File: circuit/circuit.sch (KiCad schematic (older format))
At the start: 13 parts, among them U1 LM324

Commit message: Added decoupling capacitors to diff amp circuit
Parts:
- added C1: 1uF, symbol Device:C_Small
- added C2: 0.1uF, symbol Device:C_Small
- R3, R4: value 50K -> 10K
- R7, R8: value 50K -> 1K
- gave numbers to parts that had none: 1
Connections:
- net GND: now also C1.2, C2.2
- net VCC: now also C1.1, C2.1
- net at R4.1, R7.2: now also U1.6 (-); no longer U1.5 (+)
- net at R3.1, R8.2: now also U1.5 (+); no longer U1.6 (-)
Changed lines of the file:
@@
 U 2 1 60F7D144
 P 5400 2500
-F 0 "U1" H 5400 2867 50  0000 C CNN
-F 1 "LM324" H 5400 2776 50  0000 C CNN
+F 0 "U1" H 5400 2133 50  0000 C CNN
+F 1 "LM324" H 5400 2224 50  0000 C CNN
 F 2 "" H 5350 2600 50  0001 C CNN
 F 3 "http://www.ti.com/lit/ds/symlink/lm2902-n.pdf" H 5450 2700 50  0001 C CNN
 	2    5400 2500
-	1    0    0    -1
+	1    0    0    1
 $EndComp
 $Comp
@@
 L power:VCC #PWR08
 U 1 1 60F89E99
-P 9350 1650
-F 0 "#PWR08" H 9350 1500 50  0001 C CNN
-F 1 "VCC" H 9365 1823 50  0000 C CNN
-F 2 "" H 9350 1650 50  0001 C CNN
-F 3 "" H 9350 1650 50  0001 C CNN
-	1    9350 1650
+P 9350 800
+F 0 "#PWR08" H 9350 650 50  0001 C CNN
+F 1 "VCC" H 9365 973 50  0000 C CNN
+F 2 "" H 9350 800 50  0001 C CNN
+F 3 "" H 9350 800 50  0001 C CNN
+	1    9350 800
 	1    0    0    -1
 $EndComp
@@
 	9050 1900 9350 1900
 Wire Wire Line
-	9350 1900 9350 1650
+	9350 1900 9350 1450
 $Comp
 L Device:R_Small_US R1
@@
 P 4250 3500
 F 0 "R3" V 4045 3500 50  0000 C CNN
-F 1 "50K" V 4136 3500 50  0000 C CNN
+F 1 "10K" V 4136 3500 50  0000 C CNN
 F 2 "" H 4250 3500 50  0001 C CNN
 F 3 "~" H 4250 3500 50  0001 C CNN
@@
 P 5400 1800
 F 0 "R7" V 5195 1800 50  0000 C CNN
-F 1 "50K" V 5286 1800 50  0000 C CNN
+F 1 "1K" V 5286 1800 50  0000 C CNN
 F 2 "" H 5400 1800 50  0001 C CNN
 F 3 "~" H 5400 1800 50  0001 C CNN
@@
 P 5400 3500
 F 0 "R8" V 5195 3500 50  0000 C CNN
-F 1 "50K" V 5286 3500 50  0000 C CNN
+F 1 "1K" V 5286 3500 50  0000 C CNN
 F 2 "" H 5400 3500 50  0001 C CNN
 F 3 "~" H 5400 3500 50  0001 C CNN
@@
 P 4300 1800
 F 0 "R4" V 4095 1800 50  0000 C CNN
-F 1 "50K" V 4186 1800 50  0000 C CNN
+F 1 "10K" V 4186 1800 50  0000 C CNN
 F 2 "" H 4300 1800 50  0001 C CNN
 F 3 "~" H 4300 1800 50  0001 C CNN
@@
 Connection ~ 5950 5750
 $Comp
-L Connector:Conn_01x04_Female J?
+L Connector:Conn_01x04_Female J1
 U 1 1 60FDAFA9
 P 8850 3550
-F 0 "J?" H 8878 3526 50  0000 L CNN
+F 0 "J1" H 8878 3526 50  0000 L CNN
 F 1 "Conn_01x04_Female" H 8878 3435 50  0000 L CNN
 F 2 "" H 8850 3550 50  0001 C CNN
@@
 $EndComp
 $Comp
-L power:VCC #PWR?
+L power:VCC #PWR09
 U 1 1 60FDEBA9
 P 8300 3250
-F 0 "#PWR?" H 8300 3100 50  0001 C CNN
+F 0 "#PWR09" H 8300 3100 50  0001 C CNN
 F 1 "VCC" H 8315 3423 50  0000 C CNN
 F 2 "" H 8300 3250 50  0001 C CNN
@@
 $EndComp
 $Comp
-L power:GND #PWR?
+L power:GND #PWR010
 U 1 1 60FDF575
 P 8300 4050
-F 0 "#PWR?" H 8300 3800 50  0001 C CNN
+F 0 "#PWR010" H 8300 3800 50  0001 C CNN
 F 1 "GND" H 8305 3877 50  0000 C CNN
 F 2 "" H 8300 4050 50  0001 C CNN
@@
 Wire Wire Line
 	8200 3650 8650 3650
+$Comp
+L Device:C_Small C2
+U 1 1 60FE947A
+P 8750 1450
+F 0 "C2" V 8521 1450 50  0000 C CNN
+F 1 "0.1uF" V 8612 1450 50  0000 C CNN
+F 2 "" H 8750 1450 50  0001 C CNN
+F 3 "~" H 8750 1450 50  0001 C CNN
+	1    8750 1450
+	0    1    1    0
+$EndComp
+$Comp
+L Device:C_Small C1
+U 1 1 60FEA1F3
+P 8750 1000
+F 0 "C1" V 8521 1000 50  0000 C CNN
+F 1 "1uF" V 8612 1000 50  0000 C CNN
+F 2 "" H 8750 1000 50  0001 C CNN
+F 3 "~" H 8750 1000 50  0001 C CNN
+	1    8750 1000
+	0    1    1    0
+$EndComp
+Wire Wire Line
+	8850 1000 9350 1000
+Connection ~ 9350 1000
+Wire Wire Line
+	9350 1000 9350 800
+Wire Wire Line
+	8850 1450 9350 1450
+Connection ~ 9350 1450
+Wire Wire Line
+	9350 1450 9350 1000
+Wire Wire Line
+	8650 1450 8100 1450
+Wire Wire Line
+	8100 1450 8100 1900
+Connection ~ 8100 1900
+Wire Wire Line
+	8650 1000 8100 1000
+Wire Wire Line
+	8100 1000 8100 1450
+Connection ~ 8100 1450
 $EndSCHEMATC

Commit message: Added Offset Voltage to Op-Amp
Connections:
- net V_REF is gone; now on net GND: R4.2, U1.1, U1.12 (+), U1.2 (-), U1.9 (-)
- net OUT+: now also U1.10 (+), U1.13 (-)
- net V_IN: no longer names the net of R3.2, RV1.2
- net V_IN: no longer U1.10 (+), U1.13 (-)
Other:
- moved on the sheet: R1, R2, R3, R4, R7, R8, RV1, U1A, U1B

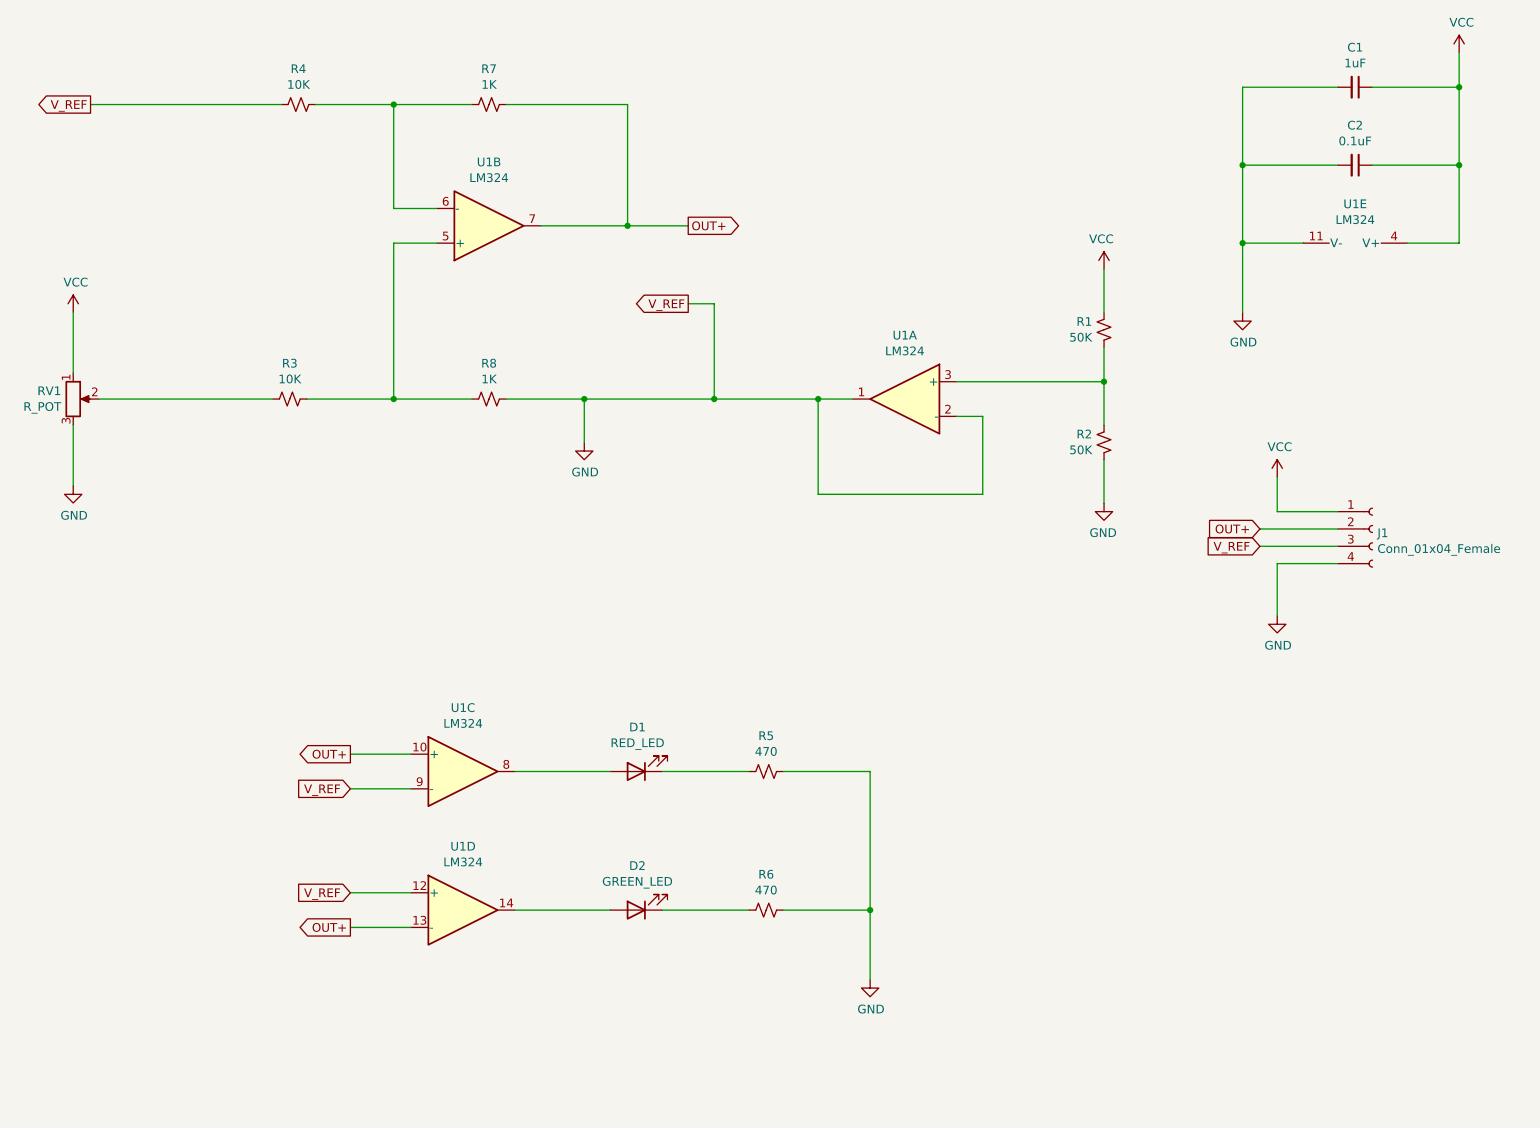
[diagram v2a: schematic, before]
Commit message: Cleaned Up Circuit Diagram
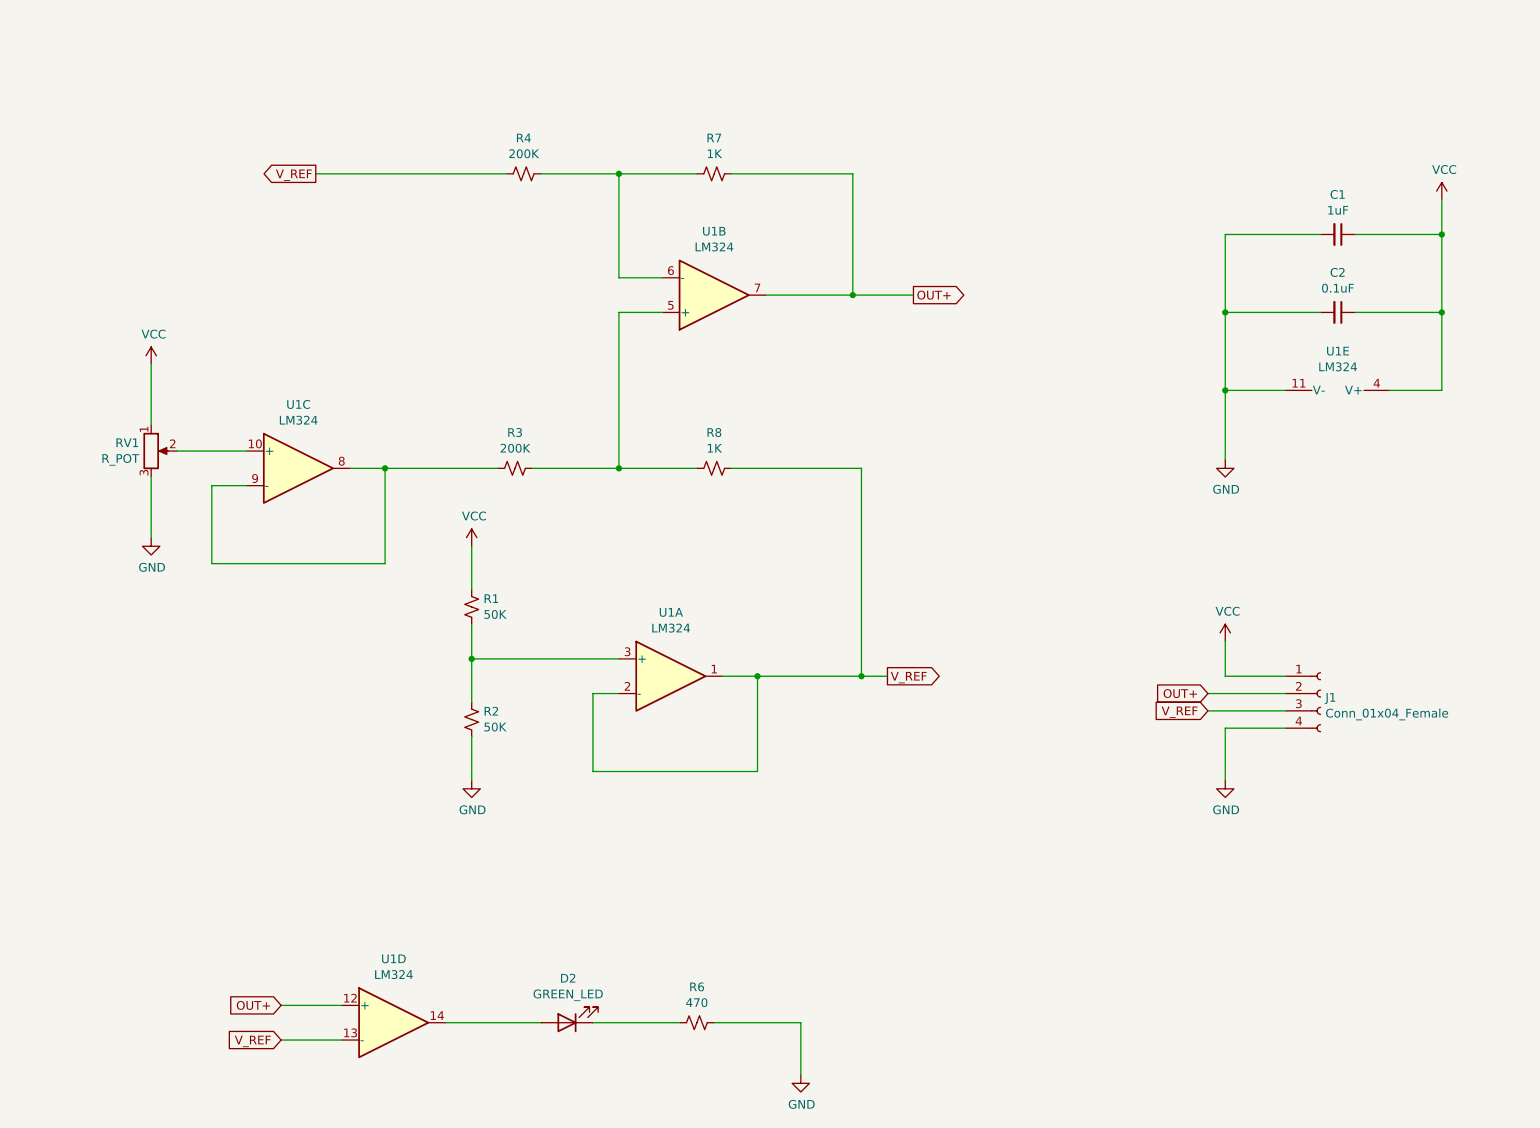
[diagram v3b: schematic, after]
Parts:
- removed D1: RED_LED, symbol Device:LED
- removed R5: 470, symbol Device:R_Small_US
- R3, R4: value 10K -> 200K
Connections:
- net GND: no longer J1.3 (Pin_3), R4.2, R8.1, U1.1, U1.12 (+), U1.2 (-), U1.9 (-)
- net OUT+: now also U1.12 (+); no longer U1.10 (+), U1.13 (-)
- net at RV1.2: now also U1.10 (+); no longer R3.2
- net at U1.8: now also R3.2, U1.9 (-)
- new net V_REF: J1.3 (Pin_3), R4.2, R8.1, U1.1, U1.13 (-), U1.2 (-)
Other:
- moved on the sheet: C1, C2, D2, J1, R1, R2, R3, R4, R6, R7, R8, RV1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

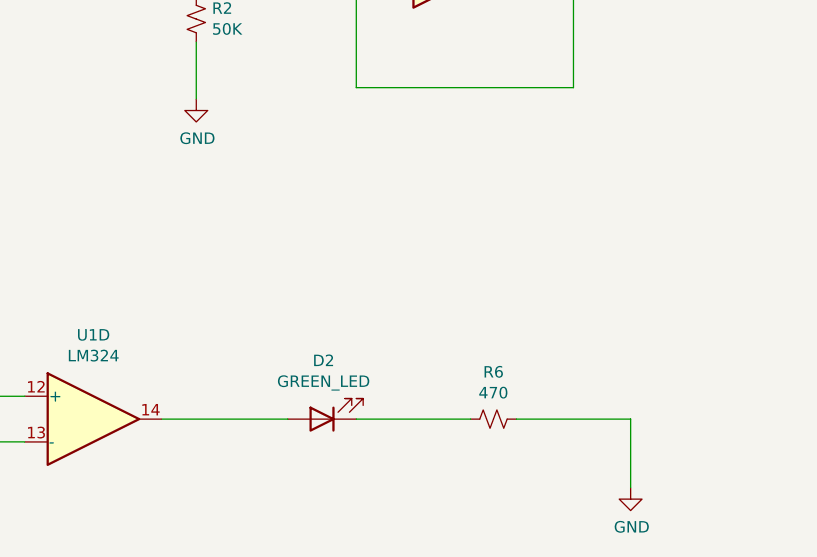
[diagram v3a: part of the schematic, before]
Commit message: Added Second Indicator LED
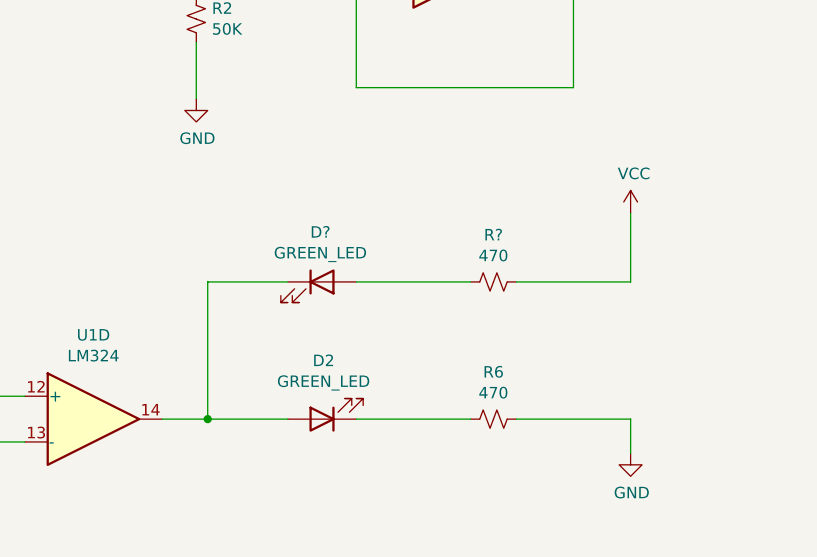
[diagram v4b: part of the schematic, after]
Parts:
- added D?: GREEN_LED, symbol Device:LED
- added R?: 470, symbol Device:R_Small_US
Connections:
- net VCC: now also R?.1
- net at D2.2 (A), U1.14: now also D?.1 (K)
- new net: D?.2 (A), R?.2
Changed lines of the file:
@@
 $EndComp
 Wire Wire Line
-	4050 6400 3500 6400
+	4050 6400 3700 6400
 Text GLabel 2550 6500 0    50   Input ~ 0
 V_REF
@@
 L power:GND #PWR06
 U 1 1 60FC7935
-P 5550 6700
-F 0 "#PWR06" H 5550 6450 50  0001 C CNN
-F 1 "GND" H 5555 6527 50  0000 C CNN
-F 2 "" H 5550 6700 50  0001 C CNN
-F 3 "" H 5550 6700 50  0001 C CNN
-	1    5550 6700
+P 5550 6550
+F 0 "#PWR06" H 5550 6300 50  0001 C CNN
+F 1 "GND" H 5555 6377 50  0000 C CNN
+F 2 "" H 5550 6550 50  0001 C CNN
+F 3 "" H 5550 6550 50  0001 C CNN
+	1    5550 6550
 	1    0    0    -1
 $EndComp
@@
 OUT+
 Wire Wire Line
-	5550 6400 5550 6700
+	5550 6400 5550 6550
 Wire Wire Line
 	1950 3100 2350 3100
@@
 	5900 4400 5900 3200
 Connection ~ 5900 4400
+$Comp
+L Device:LED D?
+U 1 1 610CE31E
+P 4200 5800
+F 0 "D?" H 4193 6017 50  0000 C CNN
+F 1 "GREEN_LED" H 4193 5926 50  0000 C CNN
+F 2 "" H 4200 5800 50  0001 C CNN
+F 3 "~" H 4200 5800 50  0001 C CNN
+	1    4200 5800
+	1    0    0    -1
+$EndComp
+$Comp
+L Device:R_Small_US R?
+U 1 1 610CF3DE
+P 4950 5800
+F 0 "R?" V 4745 5800 50  0000 C CNN
+F 1 "470" V 4836 5800 50  0000 C CNN
+F 2 "" H 4950 5800 50  0001 C CNN
+F 3 "~" H 4950 5800 50  0001 C CNN
+	1    4950 5800
+	0    1    1    0
+$EndComp
+$Comp
+L power:VCC #PWR?
+U 1 1 610D3C0A
+P 5550 5500
+F 0 "#PWR?" H 5550 5350 50  0001 C CNN
+F 1 "VCC" H 5565 5673 50  0000 C CNN
+F 2 "" H 5550 5500 50  0001 C CNN
+F 3 "" H 5550 5500 50  0001 C CNN
+	1    5550 5500
+	1    0    0    -1
+$EndComp
+Wire Wire Line
+	5550 5800 5550 5500
+Wire Wire Line
+	5050 5800 5550 5800
+Wire Wire Line
+	4350 5800 4850 5800
+Wire Wire Line
+	4050 5800 3700 5800
+Wire Wire Line
+	3700 5800 3700 6400
+Connection ~ 3700 6400
+Wire Wire Line
+	3700 6400 3500 6400
 $EndSCHEMATC

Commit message: Adjusted for final component values
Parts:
- R3, R4: value 200K -> 220K
- R7, R8: value 1K -> 2.2K
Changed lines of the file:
@@
 P 3900 3200
 F 0 "R3" V 3695 3200 50  0000 C CNN
-F 1 "200K" V 3786 3200 50  0000 C CNN
+F 1 "220K" V 3786 3200 50  0000 C CNN
 F 2 "" H 3900 3200 50  0001 C CNN
 F 3 "~" H 3900 3200 50  0001 C CNN
@@
 P 5050 1500
 F 0 "R7" V 4845 1500 50  0000 C CNN
-F 1 "1K" V 4936 1500 50  0000 C CNN
+F 1 "2.2K" V 4936 1500 50  0000 C CNN
 F 2 "" H 5050 1500 50  0001 C CNN
 F 3 "~" H 5050 1500 50  0001 C CNN
@@
 P 5050 3200
 F 0 "R8" V 4845 3200 50  0000 C CNN
-F 1 "1K" V 4936 3200 50  0000 C CNN
+F 1 "2.2K" V 4936 3200 50  0000 C CNN
 F 2 "" H 5050 3200 50  0001 C CNN
 F 3 "~" H 5050 3200 50  0001 C CNN
@@
 P 3950 1500
 F 0 "R4" V 3745 1500 50  0000 C CNN
-F 1 "200K" V 3836 1500 50  0000 C CNN
+F 1 "220K" V 3836 1500 50  0000 C CNN
 F 2 "" H 3950 1500 50  0001 C CNN
 F 3 "~" H 3950 1500 50  0001 C CNN

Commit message: Updated Readme and Added Image of Circuit Diagram
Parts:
- R1: value 50K -> 5.1K
- R2: value 50K -> 3.3K
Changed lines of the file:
@@
 P 3650 4650
 F 0 "R2" H 3718 4696 50  0000 L CNN
-F 1 "50K" H 3718 4605 50  0000 L CNN
+F 1 "3.3K" H 3718 4605 50  0000 L CNN
 F 2 "" H 3650 4650 50  0001 C CNN
 F 3 "~" H 3650 4650 50  0001 C CNN
@@
 P 3650 4000
 F 0 "R1" H 3718 4046 50  0000 L CNN
-F 1 "50K" H 3718 3955 50  0000 L CNN
+F 1 "5.1K" H 3718 3955 50  0000 L CNN
 F 2 "" H 3650 4000 50  0001 C CNN
 F 3 "~" H 3650 4000 50  0001 C CNN

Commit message: Added Background Color to Schematic
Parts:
- gave numbers to parts that had none: 2
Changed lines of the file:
@@
 encoding utf-8
 Sheet 1 1
-Title ""
-Date ""
-Rev ""
+Title "Differential Signal Generator"
+Date "2021-07-22"
+Rev "1.0"
 Comp ""
 Comment1 ""
@@
 Connection ~ 5900 4400
 $Comp
-L Device:LED D?
+L Device:LED D1
 U 1 1 610CE31E
 P 4200 5800
-F 0 "D?" H 4193 6017 50  0000 C CNN
+F 0 "D1" H 4193 6017 50  0000 C CNN
 F 1 "GREEN_LED" H 4193 5926 50  0000 C CNN
 F 2 "" H 4200 5800 50  0001 C CNN
@@
 $EndComp
 $Comp
-L Device:R_Small_US R?
+L Device:R_Small_US R5
 U 1 1 610CF3DE
 P 4950 5800
-F 0 "R?" V 4745 5800 50  0000 C CNN
+F 0 "R5" V 4745 5800 50  0000 C CNN
 F 1 "470" V 4836 5800 50  0000 C CNN
 F 2 "" H 4950 5800 50  0001 C CNN
@@
 $EndComp
 $Comp
-L power:VCC #PWR?
+L power:VCC #PWR05
 U 1 1 610D3C0A
 P 5550 5500
-F 0 "#PWR?" H 5550 5350 50  0001 C CNN
+F 0 "#PWR05" H 5550 5350 50  0001 C CNN
 F 1 "VCC" H 5565 5673 50  0000 C CNN
 F 2 "" H 5550 5500 50  0001 C CNN
